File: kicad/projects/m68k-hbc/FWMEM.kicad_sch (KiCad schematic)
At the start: 2 parts, among them U28 FWMC

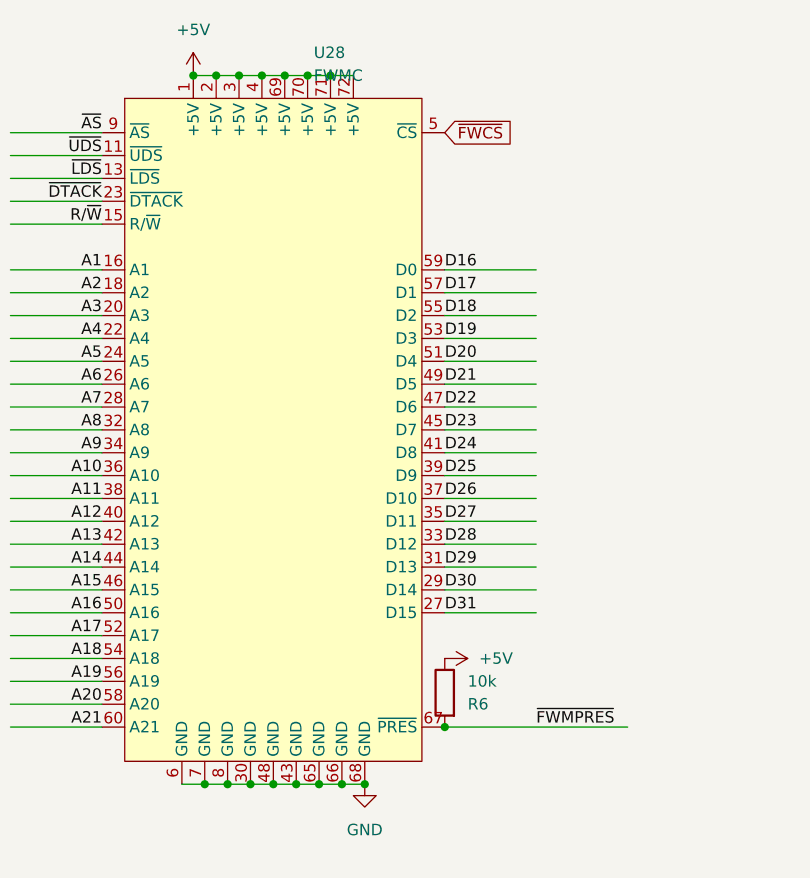
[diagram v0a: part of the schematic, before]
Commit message: Modified system architecture, New KiCad Project: Cache Memory Module(SIMM80)
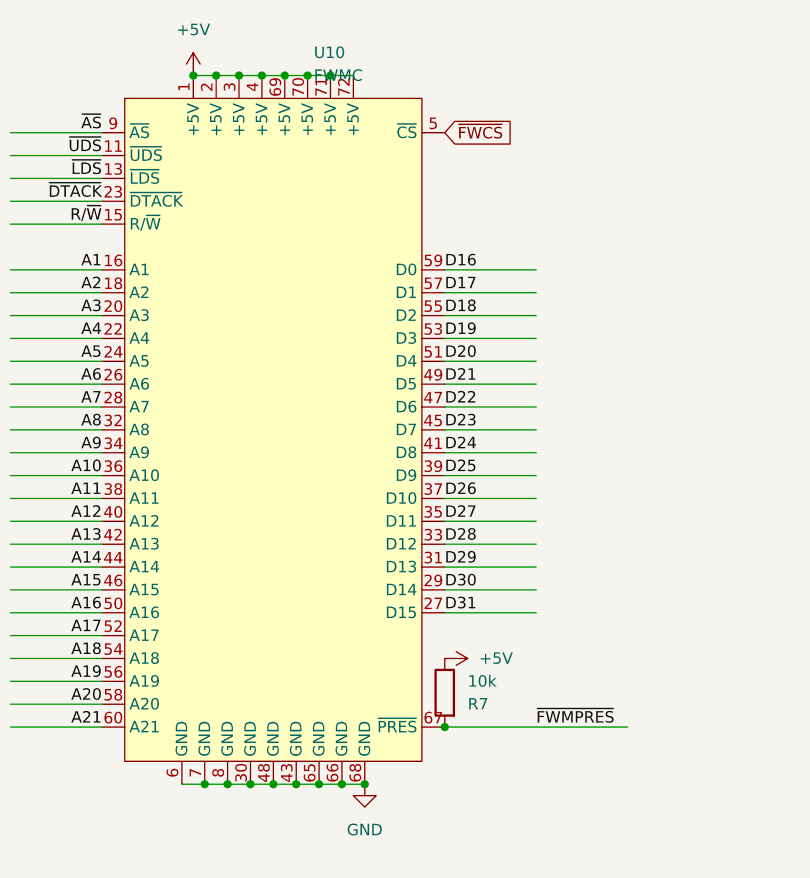
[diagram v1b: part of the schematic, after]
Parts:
- renumbered R6 to R7, U28 to U10
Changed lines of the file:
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@@
   (symbol (lib_id "power:+5V") (at 144.78 119.38 270) (unit 1)
     (in_bom yes) (on_board yes) (dnp no) (fields_autoplaced)
-    (property "Reference" "#PWR0219" (at 140.97 119.38 0)
+    (property "Reference" "#PWR0156" (at 140.97 119.38 0)
       (effects (font (size 1.27 1.27)) hide)
     )
@@
       (project "m68k-hbc"
         (path "/da427610-5b61-43bd-a536-c238ace8bf3f/6361ff15-960f-4c03-97f8-c94d1c01b620"
-          (reference "#PWR0219") (unit 1)
+          (reference "#PWR0156") (unit 1)
         )
       )
@@
         )
         (path "/da427610-5b61-43bd-a536-c238ace8bf3f/6361ff15-960f-4c03-97f8-c94d1c01b620"
-          (reference "#PWR0220") (unit 1)
+          (reference "#PWR0157") (unit 1)
         )
       )
@@
   (symbol (lib_id "Device:R") (at 144.78 123.19 0) (mirror y) (unit 1)
     (in_bom yes) (on_board yes) (dnp no)
-    (property "Reference" "R6" (at 147.32 124.46 0)
+    (property "Reference" "R7" (at 147.32 124.46 0)
       (effects (font (size 1.27 1.27)) (justify right))
     )
@@
       (project "m68k-hbc"
         (path "/da427610-5b61-43bd-a536-c238ace8bf3f/6361ff15-960f-4c03-97f8-c94d1c01b620"
-          (reference "R6") (unit 1)
+          (reference "R7") (unit 1)
         )
       )
@@
   (symbol (lib_id "FWMC:FWMC") (at 125.73 93.98 0) (unit 1)
     (in_bom yes) (on_board yes) (dnp no) (fields_autoplaced)
-    (property "Reference" "U28" (at 130.2259 52.07 0)
+    (property "Reference" "U10" (at 130.2259 52.07 0)
       (effects (font (size 1.27 1.27)) (justify left))
     )
@@
       (project "m68k-hbc"
         (path "/da427610-5b61-43bd-a536-c238ace8bf3f/6361ff15-960f-4c03-97f8-c94d1c01b620"
-          (reference "U28") (unit 1)
+          (reference "U10") (unit 1)
         )
       )
@@
         )
         (path "/da427610-5b61-43bd-a536-c238ace8bf3f/6361ff15-960f-4c03-97f8-c94d1c01b620"
-          (reference "#PWR0218") (unit 1)
+          (reference "#PWR0155") (unit 1)
         )
       )

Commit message: Some Updates
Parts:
- removed R7: 10k, Resistor_SMD:R_1206_3216Metric_Pad1.30x1.75mm_HandSolder, symbol Device:R
- removed U10: FWMC, 55308438:55308438, symbol FWMC:FWMC
- added IC3: 23LCV1024-I_SN, Package_SO:SOIC-8_3.9x4.9mm_P1.27mm, symbol 23LCV1024-I_SN:23LCV1024-I_SN
- added U6, U7: SST39SF040, Package_DIP:DIP-32_W15.24mm_Socket, symbol Memory_Flash:SST39SF040
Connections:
- net A1: now also U6.12 (A0), U7.12 (A0)
- net A10: now also U6.26 (A9), U7.26 (A9)
- net A11: now also U6.23 (A10), U7.23 (A10)
- net A12: now also U6.25 (A11), U7.25 (A11)
- net A13: now also U6.4 (A12), U7.4 (A12)
- net A14: now also U6.28 (A13), U7.28 (A13)
- net A15: now also U6.29 (A14), U7.29 (A14)
- net A16: now also U6.3 (A15), U7.3 (A15)
- net A17: now also U6.2 (A16), U7.2 (A16)
- net A18: now also U6.30 (A17), U7.30 (A17)
- net A19: now also U6.1 (A18), U7.1 (A18)
- net A2: now also U6.11 (A1), U7.11 (A1)
- net A3: now also U6.10 (A2), U7.10 (A2)
- net A4: now also U6.9 (A3), U7.9 (A3)
- net A5: now also U6.8 (A4), U7.8 (A4)
- net A6: now also U6.7 (A5), U7.7 (A5)
- net A7: now also U6.6 (A6), U7.6 (A6)
- net A8: now also U6.5 (A7), U7.5 (A7)
- net A9: now also U6.27 (A8), U7.27 (A8)
- net D16: now also U6.13 (D0)
- net D17: now also U6.14 (D1)
- net D18: now also U6.15 (D2)
- net D19: now also U6.17 (D3)
- net D20: now also U6.18 (D4)
- net D21: now also U6.19 (D5)
- net D22: now also U6.20 (D6)
- net D23: now also U6.21 (D7)
- net D24: now also U7.13 (D0)
- net D25: now also U7.14 (D1)
- net D26: now also U7.15 (D2)
- net D27: now also U7.17 (D3)
- net D28: now also U7.18 (D4)
- net D29: now also U7.19 (D5)
- net D30: now also U7.20 (D6)
- net D31: now also U7.21 (D7)
- net GND: now also IC3.4 (VSS), U6.16 (GND), U7.16 (GND)
- net R/~{W}: now also U6.24 (OE), U7.24 (OE)
- new net +BATT: IC3.7 (VBAT)
- new net PWR_CPURAM: IC3.8 (VCC), U6.32 (VCC), U7.32 (VCC)
- new net SYS_MISO: IC3.2 (SO/SIO1)
- new net SYS_MOSI: IC3.5 (SI/SIO0)
- new net SYS_SCK: IC3.6 (SCK)
- new net ~{CS_FWM}: U6.22 (CE), U7.22 (CE)
- new net ~{CS_NVRAM}: IC3.1 (~{CS})
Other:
- note added: "Local Bus Signals"
- note added: "System Serial Bus"
